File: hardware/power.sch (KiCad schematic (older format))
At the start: 21 parts

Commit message: changed heirarchy labels, changed diode and inductor to standard library symbols
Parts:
- removed L?: NP06DZB6RM8, symbol NP06DZB6RM8
- removed d?: DFLS240L, symbol DFLS240L
- added D?: DFLS240L, symbol DIODESCH
- added L?: NP06DZB6RM8, symbol INDUCTOR
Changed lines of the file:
@@
-EESchema Schematic File Version 2  date Thu 31 Oct 2013 01:30:22 PM EDT
+EESchema Schematic File Version 2  date Mon 04 Nov 2013 07:38:03 AM EST
 LIBS:power
 LIBS:device
@@
 Sheet 2 5
 Title ""
-Date "31 oct 2013"
+Date "4 nov 2013"
 Rev ""
 Comp ""
@@
 Comment4 ""
 $EndDescr
+Wire Wire Line
+	6550 2500 7000 2500
+Wire Wire Line
+	8300 5350 7950 5350
+Connection ~ 8150 4350
+Wire Wire Line
+	8150 4750 8150 4350
+Connection ~ 9050 6400
+Wire Wire Line
+	9050 6400 7950 6400
+Wire Wire Line
+	7950 6400 7950 6200
+Wire Wire Line
+	7950 4650 7950 4750
+Wire Wire Line
+	7700 5350 7700 5550
+Wire Wire Line
+	7700 5550 8300 5550
+Connection ~ 10150 4350
+Wire Wire Line
+	9050 4800 9050 4350
+Wire Wire Line
+	10150 4250 10150 4650
+Wire Wire Line
+	9800 5450 10550 5450
+Wire Wire Line
+	10400 1750 10400 2200
+Wire Wire Line
+	10400 2200 7500 2200
+Wire Wire Line
+	9400 1250 10850 1250
+Connection ~ 9800 1250
+Wire Wire Line
+	9800 1250 9800 1350
+Connection ~ 7950 1250
+Wire Wire Line
+	7950 1250 7950 1650
+Wire Wire Line
+	7950 1650 8200 1650
+Wire Wire Line
+	8800 2450 8800 1950
+Wire Wire Line
+	8200 1250 3800 1250
+Connection ~ 7000 2500
+Connection ~ 5300 2500
+Wire Wire Line
+	4800 3450 4800 2500
+Wire Wire Line
+	4800 3450 4350 3450
+Wire Wire Line
+	5300 3050 5300 3250
+Connection ~ 1850 5050
+Wire Wire Line
+	1300 5050 7000 5050
+Connection ~ 1850 2750
+Wire Wire Line
+	1850 4000 1850 2750
+Connection ~ 3050 5050
+Wire Wire Line
+	3050 5050 3050 3650
+Wire Wire Line
+	3050 3650 3150 3650
+Wire Wire Line
+	2800 4050 2800 3550
+Wire Wire Line
+	2800 3550 3150 3550
+Wire Wire Line
+	2400 3800 2400 3450
+Wire Wire Line
+	2400 3450 3150 3450
+Wire Wire Line
+	1850 5050 1850 4400
+Connection ~ 7000 3600
+Wire Wire Line
+	7000 1100 7000 4000
+Connection ~ 3750 5050
+Wire Wire Line
+	4550 4450 4550 5050
+Connection ~ 4550 3600
+Wire Wire Line
+	4550 3950 4550 3600
+Wire Wire Line
+	5550 3600 4350 3600
+Wire Wire Line
+	7000 3600 6050 3600
+Wire Wire Line
+	3750 5250 3750 3950
+Wire Wire Line
+	7000 5050 7000 4400
+Connection ~ 4550 5050
+Wire Wire Line
+	2400 5050 2400 4750
+Connection ~ 2400 5050
+Wire Wire Line
+	2400 4300 2400 4350
+Wire Wire Line
+	2800 5050 2800 4550
+Connection ~ 2800 5050
+Wire Wire Line
+	1350 2750 3700 2750
+Wire Wire Line
+	3700 2750 3700 3050
+Wire Wire Line
+	3800 1250 3800 3050
+Connection ~ 7000 1250
+Wire Wire Line
+	4350 3350 4550 3350
+Wire Wire Line
+	4550 3350 4550 1500
+Wire Wire Line
+	4550 1500 5300 1500
+Wire Wire Line
+	5300 1500 5300 1900
+Wire Wire Line
+	5300 2650 5300 2300
+Wire Wire Line
+	4800 2500 5950 2500
+Wire Wire Line
+	3150 3350 2950 3350
+Wire Wire Line
+	2950 3350 2950 2750
+Connection ~ 2950 2750
+Wire Wire Line
+	7500 1250 7500 1500
+Connection ~ 7500 1250
+Wire Wire Line
+	7500 2200 7500 1900
+Connection ~ 8800 2200
+Wire Wire Line
+	10850 1250 10850 1100
+Wire Wire Line
+	9400 1650 9500 1650
+Wire Wire Line
+	9500 1650 9500 1850
+Wire Wire Line
+	9500 1850 9800 1850
+Wire Wire Line
+	9800 1850 9800 1750
+Wire Wire Line
+	10400 1350 10400 1250
+Connection ~ 10400 1250
+Wire Wire Line
+	10150 5150 10150 5450
+Connection ~ 10150 5450
+Wire Wire Line
+	9050 6100 9050 6500
+Wire Wire Line
+	10150 4350 7700 4350
+Wire Wire Line
+	7700 4350 7700 4850
+Connection ~ 9050 4350
+Wire Wire Line
+	7950 5700 7950 5250
+Connection ~ 7950 5350
+Wire Wire Line
+	8150 5250 8150 5350
 Connection ~ 8150 5350
-Wire Wire Line
-	8150 5250 8150 5350
-Connection ~ 7950 5350
-Wire Wire Line
-	7950 5700 7950 5250
-Connection ~ 9050 4350
-Wire Wire Line
-	7700 4850 7700 4350
-Wire Wire Line
-	7700 4350 10150 4350
-Wire Wire Line
-	9050 6100 9050 6500
-Connection ~ 10150 5450
-Wire Wire Line
-	10150 5150 10150 5450
-Connection ~ 10400 1250
-Wire Wire Line
-	10400 1350 10400 1250
-Wire Wire Line
-	9800 1750 9800 1850
-Wire Wire Line
-	9800 1850 9500 1850
-Wire Wire Line
-	9500 1850 9500 1650
-Wire Wire Line
-	9500 1650 9400 1650
-Wire Wire Line
-	10850 1100 10850 1250
-Connection ~ 8800 2200
-Wire Wire Line
-	7500 1900 7500 2200
-Connection ~ 7500 1250
-Wire Wire Line
-	7500 1250 7500 1500
-Connection ~ 2950 2750
-Wire Wire Line
-	2950 2750 2950 3350
-Wire Wire Line
-	2950 3350 3150 3350
-Wire Wire Line
-	5950 2500 4800 2500
-Wire Wire Line
-	5300 2650 5300 2300
-Wire Wire Line
-	5300 1900 5300 1500
-Wire Wire Line
-	5300 1500 4550 1500
-Wire Wire Line
-	4550 1500 4550 3350
-Wire Wire Line
-	4550 3350 4350 3350
-Connection ~ 7000 1250
-Wire Wire Line
-	3800 3050 3800 1250
-Wire Wire Line
-	3700 3050 3700 2750
-Wire Wire Line
-	3700 2750 1350 2750
-Connection ~ 2800 5050
-Wire Wire Line
-	2800 5050 2800 4550
-Wire Wire Line
-	2400 4300 2400 4350
-Connection ~ 2400 5050
-Wire Wire Line
-	2400 5050 2400 4750
-Connection ~ 4550 5050
-Wire Wire Line
-	7000 4400 7000 5050
-Wire Wire Line
-	3750 5250 3750 3950
-Wire Wire Line
-	7000 3600 6050 3600
-Wire Wire Line
-	5550 3600 4350 3600
-Wire Wire Line
-	4550 3950 4550 3600
-Connection ~ 4550 3600
-Wire Wire Line
-	4550 4450 4550 5050
-Connection ~ 3750 5050
-Wire Wire Line
-	7000 1100 7000 4000
-Connection ~ 7000 3600
-Wire Wire Line
-	1850 5050 1850 4400
-Wire Wire Line
-	3150 3450 2400 3450
-Wire Wire Line
-	2400 3450 2400 3800
-Wire Wire Line
-	3150 3550 2800 3550
-Wire Wire Line
-	2800 3550 2800 4050
-Wire Wire Line
-	3150 3650 3050 3650
-Wire Wire Line
-	3050 3650 3050 5050
-Connection ~ 3050 5050
-Wire Wire Line
-	1850 4000 1850 2750
-Connection ~ 1850 2750
-Wire Wire Line
-	7000 5050 1300 5050
-Connection ~ 1850 5050
-Wire Wire Line
-	5300 3250 5300 3450
-Wire Wire Line
-	4350 3450 4800 3450
-Wire Wire Line
-	4800 3450 4800 2500
-Connection ~ 5300 2500
-Wire Wire Line
-	7000 2500 6500 2500
-Connection ~ 7000 2500
-Wire Wire Line
-	3800 1250 8200 1250
-Wire Wire Line
-	8800 2450 8800 1950
-Wire Wire Line
-	8200 1650 7950 1650
-Wire Wire Line
-	7950 1650 7950 1250
-Connection ~ 7950 1250
-Wire Wire Line
-	9800 1250 9800 1350
-Connection ~ 9800 1250
-Wire Wire Line
-	10850 1250 9400 1250
-Wire Wire Line
-	7500 2200 10400 2200
-Wire Wire Line
-	10400 2200 10400 1750
-Wire Wire Line
-	9800 5450 10550 5450
-Wire Wire Line
-	10150 4250 10150 4650
-Wire Wire Line
-	9050 4800 9050 4350
-Connection ~ 10150 4350
-Wire Wire Line
-	8300 5550 7700 5550
-Wire Wire Line
-	7700 5550 7700 5350
-Wire Wire Line
-	7950 4650 7950 4750
-Wire Wire Line
-	7950 6200 7950 6400
-Wire Wire Line
-	7950 6400 9050 6400
-Connection ~ 9050 6400
-Wire Wire Line
-	8150 4750 8150 4350
-Connection ~ 8150 4350
-Wire Wire Line
-	8300 5350 7950 5350
+$Comp
+L INDUCTOR L?
+U 1 1 52779419
+P 6250 2500
+F 0 "L?" V 6200 2500 40  0000 C CNN
+F 1 "NP06DZB6RM8" V 6350 2500 40  0000 C CNN
+	1    6250 2500
+	0    -1   -1   0
+$EndComp
+$Comp
+L DIODESCH D?
+U 1 1 5277935F
+P 5300 2850
+F 0 "D?" H 5300 2950 40  0000 C CNN
+F 1 "DFLS240L" H 5300 2750 40  0000 C CNN
+	1    5300 2850
+	0    -1   -1   0
+$EndComp
 $Comp
 L R R?
@@
 $EndComp
 $Comp
-L NP06DZB6RM8 L?
-U 1 1 526DA38E
-P 6300 2500
-F 0 "L?" H 6050 2600 60  0000 C CNN
-F 1 "NP06DZB6RM8" H 6300 2450 60  0000 C CNN
-	1    6300 2500
-	1    0    0    -1
-$EndComp
-$Comp
-L DFLS240L d?
-U 1 1 526D9F43
-P 5300 2950
-F 0 "d?" H 5500 2850 60  0000 C CNN
-F 1 "DFLS240L" H 5350 3150 60  0000 C CNN
-	1    5300 2950
-	0    -1   -1   0
-$EndComp
-$Comp
 L GND #PWR?
 U 1 1 526D9C40
-P 5300 3450
-F 0 "#PWR?" H 5300 3450 30  0001 C CNN
-F 1 "GND" H 5300 3380 30  0001 C CNN
-	1    5300 3450
-	1    0    0    -1
-$EndComp
+P 5300 3250
+F 0 "#PWR?" H 5300 3250 30  0001 C CNN
+F 1 "GND" H 5300 3180 30  0001 C CNN
+	1    5300 3250
+	1    0    0    -1
+$EndComp

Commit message: cleaned up most of the error check problems
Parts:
- removed U?: LT1761, symbol LT1761
- added U2: LT1761_1, symbol LT1761_1
- gave numbers to parts that had none: 20
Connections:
- wire segments 66 -> 95

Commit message: changed power supply to a lower cost TI part.  Still some DRC errors.
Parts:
- removed D1: DFLS240L, symbol DIODESCH
- removed R8: DNI, symbol R
- removed U1: LT1912, symbol LT1912
- added C26: 10 uF, symbol C
- added C27: 0.1 uF, symbol C
- added C28: 1.0 uF, symbol C
- added C29, C30: 20 uF, symbol C
- added U1: TPS54526_PWP, symbol TPS54526_PWP
- C1: value 4.7 uF -> 10 pF
- C2: value 470 pF -> 8200 pF
- C3: value 0.47 uF -> 0.1 uF
- C4: value 47 uF -> 10 uF
- L1: value NP06DZB6RM8 -> 3.3 uH
- R1: value 16.2k -> 0
- R2: value 68.1k -> 124K
- R3: value 100K -> 22.1K
- R4: value 536K -> 100 K
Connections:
- wire segments 95 -> 79
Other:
- moved on the sheet: C2, C3, C5, C6, C7, L1, R1, R2, R3, R5, R6, R7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

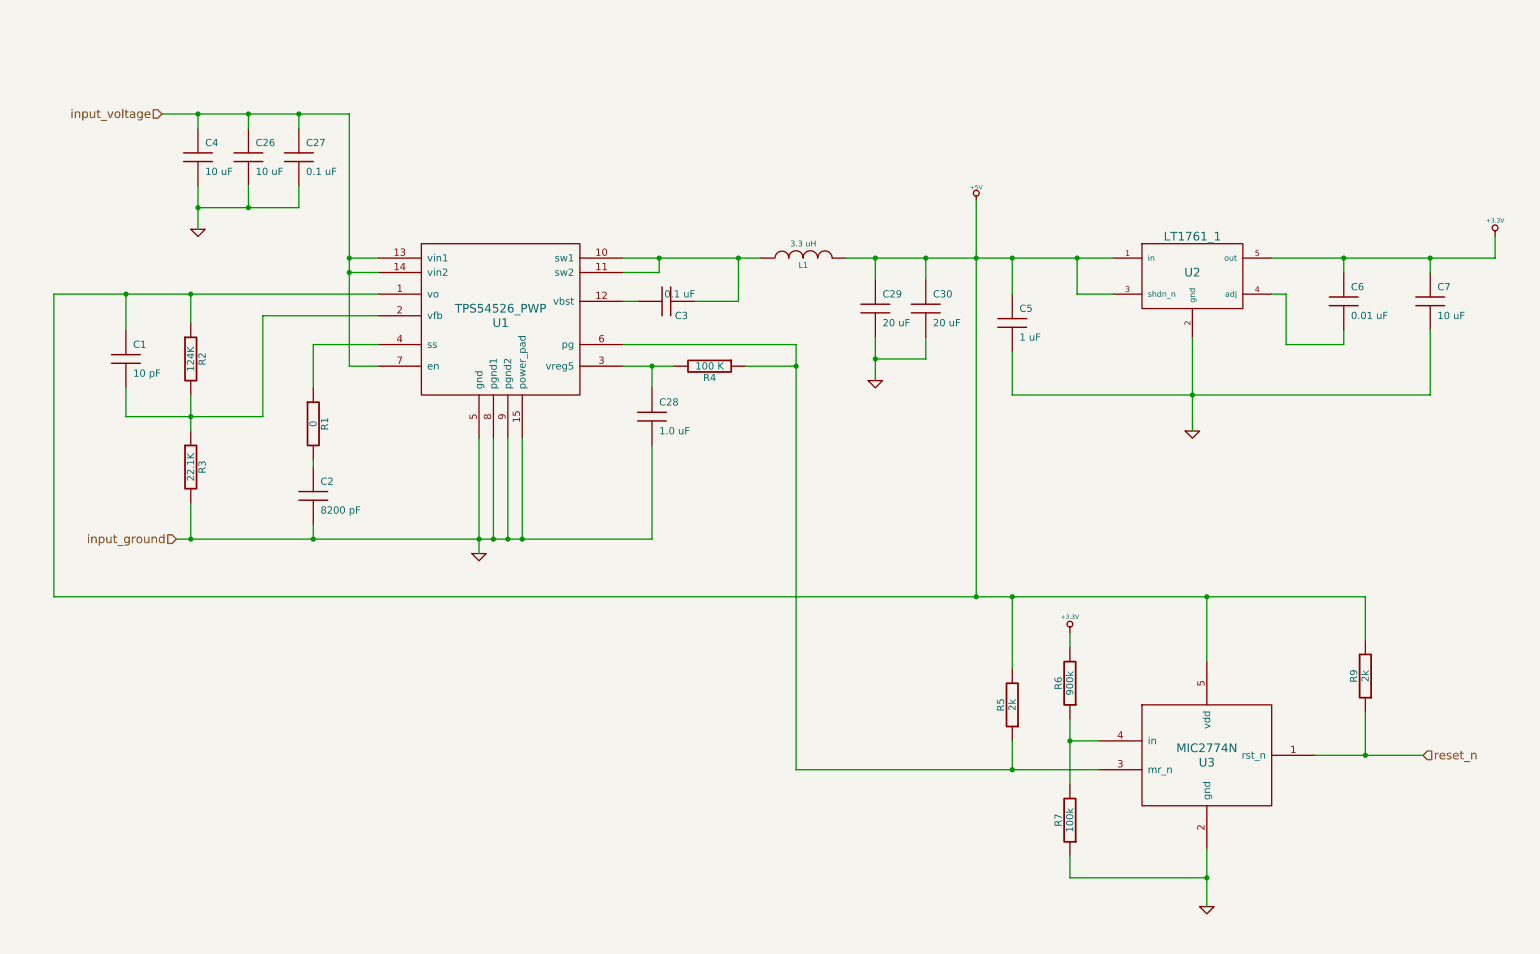
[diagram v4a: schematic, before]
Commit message: added over voltage an reverse voltage protection, fixed some DRC errors
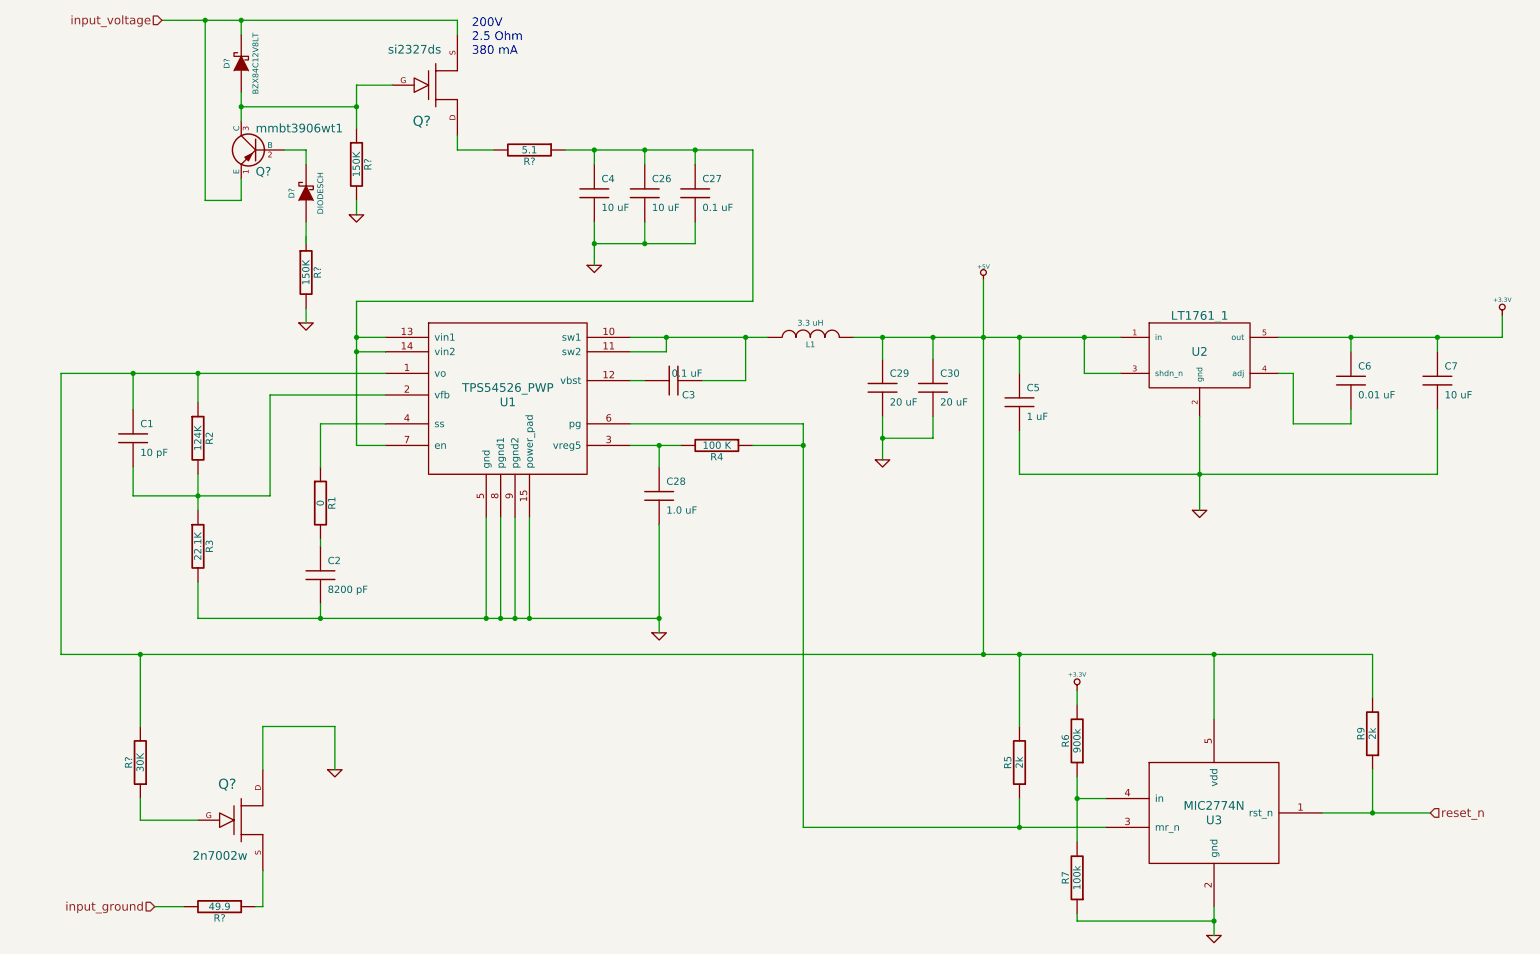
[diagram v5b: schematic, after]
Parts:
- added D?: DIODESCH, symbol DIODESCH
- added D?: BZX84C12V8LT, symbol DIODESCH
- added Q?: mmbt3906wt1, symbol PNP
- added Q?: 2n7002w, symbol FET_N
- added Q?: si2327ds, symbol FET_N
- added R?: 30K, symbol R
- added R?: 49.9, symbol R
- added R? (x2): 150K, symbol R
- added R?: 5.1, symbol R
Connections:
- net +5V: now also R?.2
- net GND: now also Q?.D, R?.2, R?.2
- net input_voltage: now also D?.2 (K), Q?.1 (E), Q?.S; no longer C26.1, C27.1, C4.1, U1.13 (vin1), U1.14 (vin2), U1.7 (en)
- new net: C26.1, C27.1, C4.1, R?.1, U1.13 (vin1), U1.14 (vin2), U1.7 (en)
- new net: D?.2 (K), Q?.2 (B)
- new net: D?.1 (A), Q?.3 (C), Q?.G, R?.1
- new net: Q?.G, R?.1
- new net: Q?.S, R?.1
- new net: Q?.D, R?.2
- new net input_ground: R?.2
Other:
- note added: "200V \n2.5 Ohm \n380 mA"
- moved on the sheet: C1, C2, C26, C27, C28, C29, C3, C30, C4, C5, C6, C7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
